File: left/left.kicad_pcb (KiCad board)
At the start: 2 copper layers, 51 parts, among them J1 USB_C_Receptacle_USB2.0_16P, SW1 SW_Push, SW2 SW_SPDT, U1 STM32G0B1CBTx, U2 SRV05-4, U3 XC6206P332MR

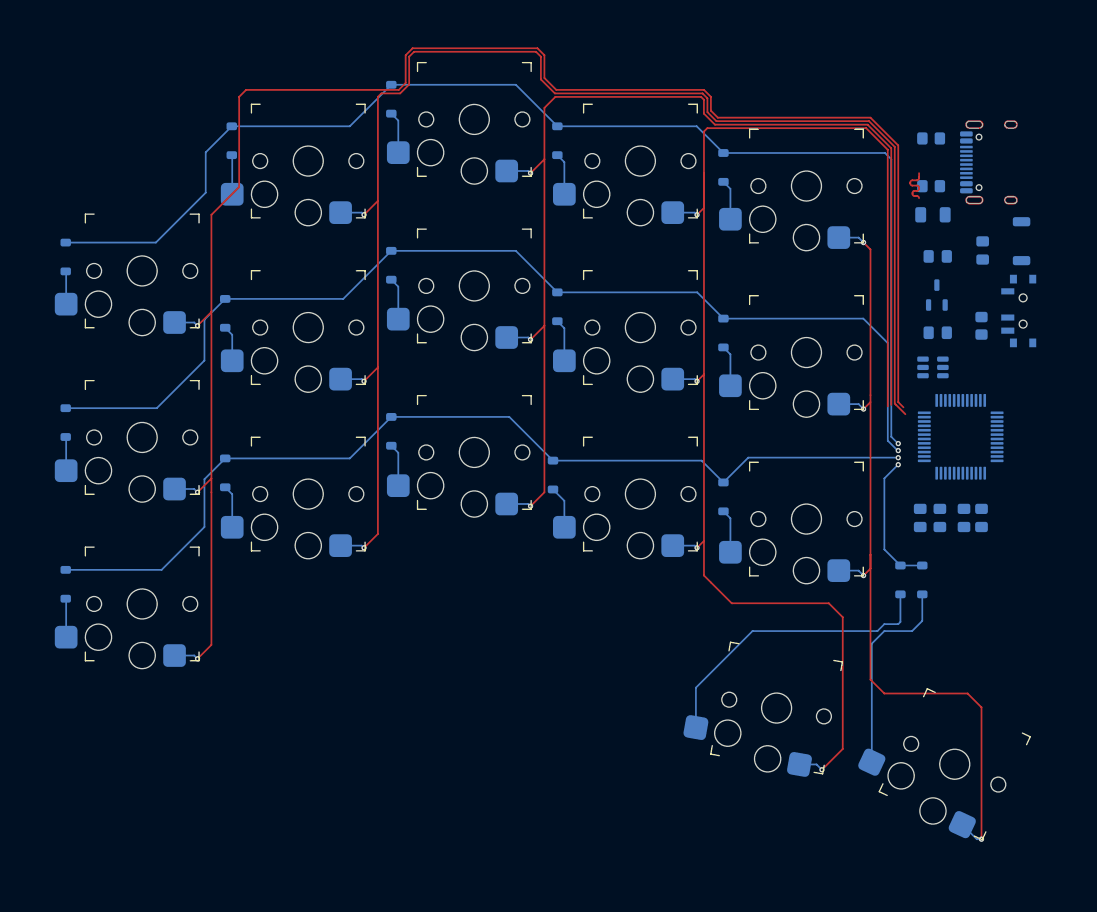
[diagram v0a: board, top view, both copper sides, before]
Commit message: redesigned pcb
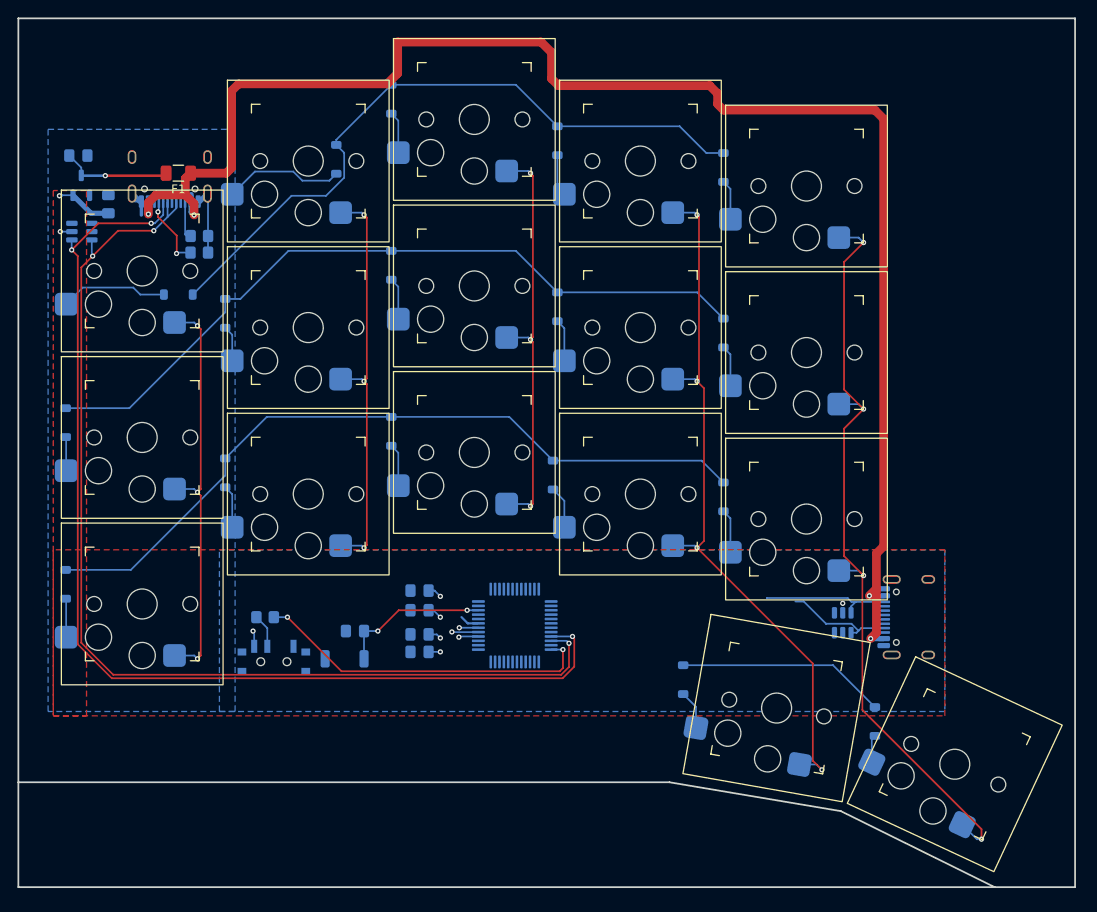
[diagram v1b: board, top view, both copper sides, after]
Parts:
- added J2: USB_C_Receptacle_OUT, Connector_USB:USB_C_Receptacle_HRO_TYPE-C-31-M-12, B.Cu at (146.1, 112.7)
- added U4: SRV05-4, Package_TO_SOT_SMD:SOT-23-6, B.Cu at (50.3, 68.6)
- F1: moved to F.Cu
- J1: value USB_C_Receptacle_USB2.0_16P -> USB_C_Receptacle_IN
- KEY1, KEY10, KEY11, KEY12, KEY13, KEY14, KEY15, KEY16, KEY17, KEY2, KEY3, KEY4, KEY5, KEY6, KEY7, KEY8, KEY9: footprint Low Profile Keyswitches:SW_Kailh_Choc_V1_HotSwap -> Low Profile Keyswitches:SW_Kailh_Choc_V1_HotSwap_18mm_caps
- moved C6 99.0 mm to (49.9, 59.9)
- moved U3 98.7 mm to (50.2, 63.3)
- moved C7 96.0 mm to (53.3, 65.5), turned to 90 degrees
- moved J1 95.2 mm to (60.3, 61.1), turned to 0 degrees
- moved SW2 94.2 mm to (72.2, 117.5), turned to 180 degrees
- moved SW1 91.0 mm to (80.3, 117.5), turned to 180 degrees
- moved R1 88.5 mm to (71.2, 112.7), turned to 180 degrees
- moved F1 86.5 mm to (61.3, 61.9)
- moved R3 84.7 mm to (63.7, 71.0), turned to 0 degrees
- moved C5 84.0 mm to (81.5, 114.3), turned to 180 degrees
- moved R2 83.9 mm to (63.7, 69.1), turned to 0 degrees
- moved C2 66.1 mm to (88.9, 116.7), turned to 180 degrees
- moved C1 63.7 mm to (88.9, 114.7), turned to 180 degrees
- moved C4 60.5 mm to (88.9, 111.9), turned to 180 degrees
- moved C3 57.9 mm to (88.9, 109.7), turned to 180 degrees
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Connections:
- U2 pad 1: unconnected-(U2-IO1-Pad1) -> RX
- U2 pad 4: D+ -> unconnected-(U2-IO3-Pad4)
- U2 pad 5: +5V -> +3.3V
- U2 pad 6: D- -> TX
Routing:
- net VBUS: track 0.00 -> 178.6 mm, vias 0 -> 4
- net COL4: track 196.0 -> 47.1 mm
- net D-: track 0.00 -> 127.9 mm, vias 0 -> 3
- net COL3: track 166.3 -> 47.0 mm
- net D+: track 5.46 -> 123.6 mm, vias 0 -> 3
- net COL2: track 132.2 -> 47.0 mm
- net COL1: track 157.5 -> 81.7 mm
- net ROW0: track 141.0 -> 77.7 mm, vias 1 -> 0
- net BOOT0: track 0.00 -> 39.3 mm, vias 0 -> 2
- net ROW1: track 121.5 -> 86.8 mm, vias 1 -> 0
- net Net-(D17-A): track 34.2 -> 4.44 mm
- net +3.3V: track 0.00 -> 23.2 mm, vias 0 -> 11
- net ROW2: track 110.0 -> 86.7 mm, vias 1 -> 0
- net Net-(D16-A): track 23.5 -> 3.15 mm
- net nRST: track 0.00 -> 17.3 mm, vias 0 -> 2
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- added copper zone on F.Cu, net +3.3V
- added copper zone on B.Cu, net GND
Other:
- board outline added: 120.9 x 99.4 mm

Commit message: should be done?
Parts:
- moved J1 1.04 mm to (60.3, 60.1)
- moved F1 0.74 mm to (61.1, 61.2)
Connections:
- U1 pad 13: ROW3 -> COL4
- U1 pad 14: ROW2 -> COL3
- U1 pad 15: ROW1 -> COL2
- U1 pad 16: ROW0 -> COL1
- U1 pad 17: unconnected-(U1-PA6-Pad17) -> COL0
- U1 pad 20: COL0 -> unconnected-(U1-PB1-Pad20)
- U1 pad 21: COL1 -> ROW0
- U1 pad 22: COL2 -> ROW1
- U1 pad 23: COL3 -> ROW2
- U1 pad 24: COL4 -> ROW3
- U1 pad 25: unconnected-(U1-PB13-Pad25) -> TX
- U1 pad 26: unconnected-(U1-PB14-Pad26) -> RX
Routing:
- net ROW0: track 77.7 -> 136.3 mm, vias 0 -> 2
- net COL0: track 89.8 -> 134.3 mm
- net COL4: track 47.1 -> 89.7 mm
- net ROW1: track 86.8 -> 126.9 mm, vias 0 -> 2
- net COL1: track 81.7 -> 112.1 mm, vias 4 -> 7
- net RX: track 12.6 -> 40.3 mm
- net TX: track 15.0 -> 39.9 mm
- net ROW3: track 23.9 -> 48.6 mm, vias 0 -> 2
- net ROW2: track 86.7 -> 108.1 mm, vias 0 -> 2
- net COL3: track 47.0 -> 64.4 mm
- net COL2: track 47.0 -> 57.6 mm
- net D+: track 123.6 -> 131.8 mm
- net GND: track 14.8 -> 9.85 mm
- net VBUS: track 178.6 -> 174.7 mm
- net D-: track 127.9 -> 130.1 mm
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
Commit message: removed warnings
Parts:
- KEY1, KEY10, KEY11, KEY12, KEY13, KEY14, KEY15, KEY16, KEY17, KEY2, KEY3, KEY4, KEY5, KEY6, KEY7, KEY8, KEY9: footprint Low Profile Keyswitches:SW_Kailh_Choc_V1_HotSwap_18mm_caps -> Low Profile Keyswitches:SW_Kailh_Choc_V1_HotSwap
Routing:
- net GND: track 9.85 -> 12.1 mm
- net COL1: vias 7 -> 6

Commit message: unverified left
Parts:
- moved C6 3.10 mm to (53.0, 59.9)
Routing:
- net VBUS: track 174.7 -> 172.8 mm
- net COL1: track 112.1 -> 113.3 mm
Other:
- board size 120.9 x 99.4 mm -> 117.6 x 97.9 mm

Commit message: fixed schematics
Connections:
- U1 pad 18: unconnected-(U1-PA7-Pad18) -> ROW0
- U1 pad 19: unconnected-(U1-PB0-Pad19) -> ROW1
- U1 pad 20: unconnected-(U1-PB1-Pad20) -> ROW2
- U1 pad 21: ROW0 -> ROW3
- U1 pad 22: ROW1 -> TX
- U1 pad 23: ROW2 -> RX
- U1 pad 24: ROW3 -> unconnected-(U1-PB12-Pad24)
- U1 pad 25: TX -> unconnected-(U1-PB13-Pad25)
- U1 pad 26: RX -> unconnected-(U1-PB14-Pad26)
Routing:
- net (no net): track 0.00 -> 24.8 mm
- net ROW3: track 48.6 -> 53.7 mm
- net TX: track 39.9 -> 45.0 mm
- net RX: track 40.3 -> 44.7 mm
- net COL1: track 113.3 -> 115.1 mm
- net COL0: track 134.3 -> 136.1 mm
- net ROW2: track 108.1 -> 106.6 mm
- net ROW1: track 126.9 -> 125.5 mm
- net ROW0: track 136.3 -> 135.3 mm
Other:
- outline, holes or cut-outs redrawn

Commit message: i dunno what i added
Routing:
- net VBUS: track 172.8 -> 172.0 mm

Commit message: v3 for left
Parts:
- F1: moved to B.Cu
- J1, J2: moved to F.Cu
- KEY1, KEY10, KEY11, KEY12, KEY13, KEY14, KEY15, KEY16, KEY17, KEY2, KEY3, KEY4, KEY5, KEY6, KEY7, KEY8, KEY9: footprint Low Profile Keyswitches:SW_Kailh_Choc_V1_HotSwap -> Keyswitch Marbastlib Choc:SW_choc_v1_HS_CPG135001S30_1u; moved to B.Cu
- moved D17 20.3 mm to (139.2, 122.5)
- moved C2 18.5 mm to (103.9, 105.8), turned to 0 degrees
- moved C1 16.5 mm to (103.9, 107.8), turned to 0 degrees
- moved C3 15.3 mm to (103.9, 112.8), turned to 0 degrees
- moved C4 15.1 mm to (103.9, 110.6), turned to 0 degrees
- moved D9 13.7 mm to (80.1, 75.1)
- moved D12 13.2 mm to (117.2, 94.1)
- moved D1 12.9 mm to (136.4, 58.9)
- moved D7 12.9 mm to (117.4, 75.0)
- moved D2 12.9 mm to (117.3, 55.9)
- moved D8 12.8 mm to (98.3, 70.3)
- moved D11 12.8 mm to (136.3, 96.9)
- moved D6 12.7 mm to (136.2, 78.0)
- moved D14 12.7 mm to (79.2, 94.1)
- moved D3 12.7 mm to (98.2, 51.4)
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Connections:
- J2 pad A6: unconnected-(J2-D+-PadA6) -> TX
- J2 pad A7: unconnected-(J2-D--PadA7) -> RX
- J2 pad A8: RX -> unconnected-(J2-SBU1-PadA8)
- J2 pad B6: unconnected-(J2-D+-PadB6) -> TX
- J2 pad B7: unconnected-(J2-D--PadB7) -> RX
- J2 pad B8: TX -> unconnected-(J2-SBU2-PadB8)
- U1 pad 13: COL4 -> unconnected-(U1-PA2-Pad13)
- U1 pad 14: COL3 -> unconnected-(U1-PA3-Pad14)
- U1 pad 15: COL2 -> unconnected-(U1-PA4-Pad15)
- U1 pad 16: COL1 -> unconnected-(U1-PA5-Pad16)
- U1 pad 17: COL0 -> unconnected-(U1-PA6-Pad17)
- U1 pad 18: ROW0 -> unconnected-(U1-PA7-Pad18)
- U1 pad 19: ROW1 -> RX
- U1 pad 20: ROW2 -> unconnected-(U1-PB1-Pad20)
- U1 pad 21: ROW3 -> TX
- U1 pad 22: TX -> COL1
- U1 pad 23: RX -> COL0
- U1 pad 24: unconnected-(U1-PB12-Pad24) -> ROW3
- U1 pad 37: unconnected-(U1-PA15-Pad37) -> COL4
- U1 pad 38: unconnected-(U1-PD0-Pad38) -> COL3
- U1 pad 39: unconnected-(U1-PD1-Pad39) -> COL2
- U1 pad 46: unconnected-(U1-PB7-Pad46) -> ROW0
- U1 pad 47: unconnected-(U1-PB8-Pad47) -> ROW1
- U1 pad 48: unconnected-(U1-PB9-Pad48) -> ROW2
- U2 pad 1: RX -> TX
- U2 pad 3: unconnected-(U2-IO2-Pad3) -> TX
- U2 pad 4: unconnected-(U2-IO3-Pad4) -> RX
- U2 pad 6: TX -> RX
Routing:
- net +3.3V: track 24.3 -> 181.4 mm, vias 11 -> 5
- net BOOT0: track 39.3 -> 6.94 mm, vias 2 -> 0
- net (no net): track 24.8 -> 0.00 mm
- net COL0: track 136.1 -> 114.1 mm, vias 4 -> 3
- net nRST: track 17.3 -> 38.4 mm
- net ROW0: track 135.3 -> 155.9 mm
- net D-: track 130.1 -> 109.7 mm, vias 3 -> 5
- net D+: track 131.8 -> 111.5 mm, vias 3 -> 4
- net COL1: track 115.1 -> 95.7 mm, vias 6 -> 3
- net TX: track 45.0 -> 59.3 mm, vias 0 -> 1
- net Net-(D16-A): track 3.15 -> 16.6 mm
- net RX: track 44.7 -> 56.5 mm, vias 0 -> 2
- net Net-(D5-A): track 12.3 -> 3.57 mm
- net ROW1: track 125.5 -> 134.1 mm
- net GND: track 12.1 -> 19.2 mm, vias 0 -> 40
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- added copper zone on F.Cu, net GND
- removed copper zone on F.Cu, net +3.3V
